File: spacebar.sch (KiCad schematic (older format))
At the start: 16 parts

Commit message: Flip some spacebars
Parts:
- K_SP1, K_SP3: footprint MX_Alps_Hybrid:MX-7U -> MX_Alps_Hybrid:MX-7U-ReversedStabilizers
- K_SP2: footprint MX_Alps_Hybrid:MX-6.25U -> MX_Alps_Hybrid:MX-6.25U-ReversedStabilizers
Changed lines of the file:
@@
 F 0 "K_SP2" H 5150 1450 60  0000 C CNN
 F 1 "MX-6.25U" H 5150 1375 20  0000 C CNN
-F 2 "MX_Alps_Hybrid:MX-6.25U" H 5125 1300 60  0001 C CNN
+F 2 "MX_Alps_Hybrid:MX-6.25U-ReversedStabilizers" H 5125 1300 60  0001 C CNN
 F 3 "" H 5125 1300 60  0001 C CNN
 	1    5150 1325
@@
 F 0 "K_SP1" H 5125 5650 60  0000 C CNN
 F 1 "MX-7U" H 5125 5575 20  0000 C CNN
-F 2 "MX_Alps_Hybrid:MX-7U" H 5100 5500 60  0001 C CNN
+F 2 "MX_Alps_Hybrid:MX-7U-ReversedStabilizers" H 5100 5500 60  0001 C CNN
 F 3 "" H 5100 5500 60  0001 C CNN
 	1    5125 5525
@@
 F 0 "K_SP3" H 5125 6175 60  0000 C CNN
 F 1 "MX-7U" H 5125 6100 20  0000 C CNN
-F 2 "MX_Alps_Hybrid:MX-7U" H 5100 6025 60  0001 C CNN
+F 2 "MX_Alps_Hybrid:MX-7U-ReversedStabilizers" H 5100 6025 60  0001 C CNN
 F 3 "" H 5100 6025 60  0001 C CNN
 	1    5125 6050

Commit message: Add dummy 6U hole schematic
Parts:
- added K_SP3_ExtraStabs: MX-6U-STABS, symbol MX-ISO
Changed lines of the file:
@@
 	5375 6525 4875 6525
 Connection ~ 4925 6450
+$Comp
+L MX-ISO K_SP3_ExtraStabs
+U 1 1 598719D6
+P 5100 7100
+F 0 "K_SP3_ExtraStabs" H 5100 7225 60  0000 C CNN
+F 1 "MX-6U-STABS" H 5100 7150 20  0000 C CNN
+F 2 "" H 5075 7075 60  0001 C CNN
+F 3 "" H 5075 7075 60  0001 C CNN
+	1    5100 7100
+	1    0    0    -1
+$EndComp
 $EndSCHEMATC

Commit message: Stack bottom row, move HHKB layout out of the way temporarily
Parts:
- removed K_SP3_ExtraStabs: MX-6U-STABS, symbol MX-ISO
- added K_SP3_Extra1: MX-6U, MX_Alps_Hybrid:MX-6U-7UOverlay, symbol MX-6U
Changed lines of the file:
@@
 Connection ~ 4925 6450
 $Comp
-L MX-ISO K_SP3_ExtraStabs
-U 1 1 598719D6
-P 5100 7100
-F 0 "K_SP3_ExtraStabs" H 5100 7225 60  0000 C CNN
-F 1 "MX-6U-STABS" H 5100 7150 20  0000 C CNN
-F 2 "" H 5075 7075 60  0001 C CNN
-F 3 "" H 5075 7075 60  0001 C CNN
-	1    5100 7100
+L MX-6U K_SP3_Extra1
+U 1 1 5987A302
+P 6725 3400
+F 0 "K_SP3_Extra1" H 6725 3525 60  0000 C CNN
+F 1 "MX-6U" H 6725 3450 20  0000 C CNN
+F 2 "MX_Alps_Hybrid:MX-6U-7UOverlay" H 6700 3375 60  0001 C CNN
+F 3 "" H 6700 3375 60  0001 C CNN
+	1    6725 3400
 	1    0    0    -1
 $EndComp

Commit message: Fix 2.25 and 2.75U flipped stabilizer holes
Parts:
- K_SP11, K_SP5, K_SP8: footprint MX_Alps_Hybrid:MX-2.75U -> MX_Alps_Hybrid:MX-2.75U-ReversedStabilizer
- K_SP6, K_SP7: footprint MX_Alps_Hybrid:MX-2.25U -> MX_Alps_Hybrid:MX-2.25U-ReversedStabilizer
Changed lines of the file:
@@
 F 0 "K_SP5" H 4700 1975 60  0000 C CNN
 F 1 "MX-2.75U" H 4700 1900 20  0000 C CNN
-F 2 "MX_Alps_Hybrid:MX-2.75U" H 4675 1825 60  0001 C CNN
+F 2 "MX_Alps_Hybrid:MX-2.75U-ReversedStabilizer" H 4675 1825 60  0001 C CNN
 F 3 "" H 4675 1825 60  0001 C CNN
 	1    4700 1850
@@
 F 0 "K_SP7" H 5600 1975 60  0000 C CNN
 F 1 "MX-2.25U" H 5600 1900 20  0000 C CNN
-F 2 "MX_Alps_Hybrid:MX-2.25U" H 5575 1825 60  0001 C CNN
+F 2 "MX_Alps_Hybrid:MX-2.25U-ReversedStabilizer" H 5575 1825 60  0001 C CNN
 F 3 "" H 5575 1825 60  0001 C CNN
 	1    5600 1850
@@
 F 0 "K_SP6" H 4700 2500 60  0000 C CNN
 F 1 "MX-2.25U" H 4700 2425 20  0000 C CNN
-F 2 "MX_Alps_Hybrid:MX-2.25U" H 4675 2350 60  0001 C CNN
+F 2 "MX_Alps_Hybrid:MX-2.25U-ReversedStabilizer" H 4675 2350 60  0001 C CNN
 F 3 "" H 4675 2350 60  0001 C CNN
 	1    4700 2375
@@
 F 0 "K_SP8" H 5600 2500 60  0000 C CNN
 F 1 "MX-2.75U" H 5600 2425 20  0000 C CNN
-F 2 "MX_Alps_Hybrid:MX-2.75U" H 5575 2350 60  0001 C CNN
+F 2 "MX_Alps_Hybrid:MX-2.75U-ReversedStabilizer" H 5575 2350 60  0001 C CNN
 F 3 "" H 5575 2350 60  0001 C CNN
 	1    5600 2375
@@
 F 0 "K_SP11" H 4700 3550 60  0000 C CNN
 F 1 "MX-2.75U" H 4700 3475 20  0000 C CNN
-F 2 "MX_Alps_Hybrid:MX-2.75U" H 4675 3400 60  0001 C CNN
+F 2 "MX_Alps_Hybrid:MX-2.75U-ReversedStabilizer" H 4675 3400 60  0001 C CNN
 F 3 "" H 4675 3400 60  0001 C CNN
 	1    4700 3425

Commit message: Get rid of LM5 and SP1 for 6.5U bottom row
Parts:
- removed K_SP1: MX-7U, MX_Alps_Hybrid:MX-7U-ReversedStabilizers, symbol MX-7U
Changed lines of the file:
@@
-$EndComp
-$Comp
-L MX-7U K_SP1
-U 1 1 594AF20B
-P 5125 5525
-F 0 "K_SP1" H 5125 5650 60  0000 C CNN
-F 1 "MX-7U" H 5125 5575 20  0000 C CNN
-F 2 "MX_Alps_Hybrid:MX-7U-ReversedStabilizers" H 5100 5500 60  0001 C CNN
-F 3 "" H 5100 5500 60  0001 C CNN
-	1    5125 5525
-	1    0    0    -1
 $EndComp
 $Comp

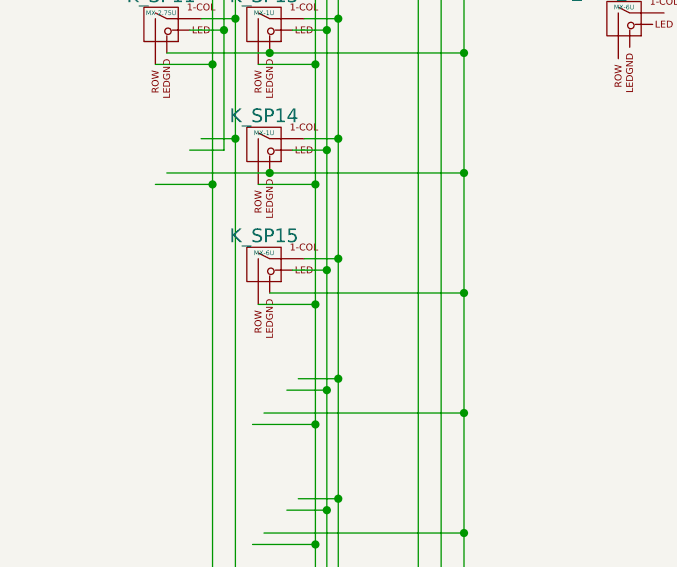
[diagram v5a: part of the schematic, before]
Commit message: Remove true HHKB row (LM8/9, SP15, RM15/16)
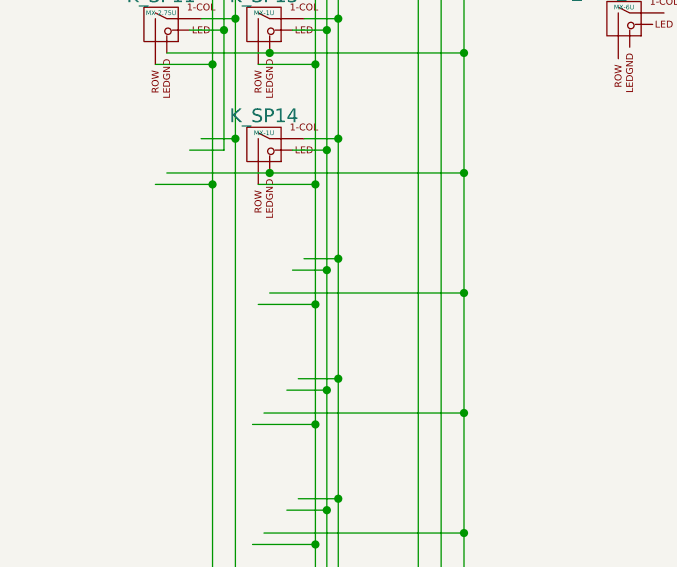
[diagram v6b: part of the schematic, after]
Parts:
- removed K_SP15: MX-6U, MX_Alps_Hybrid:MX-6U, symbol MX-6U
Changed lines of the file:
@@
-$EndComp
-$Comp
-L MX-6U K_SP15
-U 1 1 594AEB53
-P 5150 4475
-F 0 "K_SP15" H 5150 4600 60  0000 C CNN
-F 1 "MX-6U" H 5150 4525 20  0000 C CNN
-F 2 "MX_Alps_Hybrid:MX-6U" H 5125 4450 60  0001 C CNN
-F 3 "" H 5125 4450 60  0001 C CNN
-	1    5150 4475
-	1    0    0    -1
 $EndComp
 $Comp

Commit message: Remove SP14, clean up PCB
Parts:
- removed K_SP14: MX-1U, MX_Alps_Hybrid:MX-1U, symbol MX-1U
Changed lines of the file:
@@
-$EndComp
-$Comp
-L MX-2.75U K_SP5
-U 1 1 594AD90C
-P 4700 1850
-F 0 "K_SP5" H 4700 1975 60  0000 C CNN
-F 1 "MX-2.75U" H 4700 1900 20  0000 C CNN
-F 2 "MX_Alps_Hybrid:MX-2.75U-ReversedStabilizer" H 4675 1825 60  0001 C CNN
-F 3 "" H 4675 1825 60  0001 C CNN
-	1    4700 1850
-	1    0    0    -1
 $EndComp
 $Comp
@@
 F 3 "" H 5125 3400 60  0001 C CNN
 	1    5150 3425
-	1    0    0    -1
-$EndComp
-$Comp
-L MX-1U K_SP14
-U 1 1 594AE7A9
-P 5150 3950
-F 0 "K_SP14" H 5150 4075 60  0000 C CNN
-F 1 "MX-1U" H 5150 4000 20  0000 C CNN
-F 2 "MX_Alps_Hybrid:MX-1U" H 5125 3925 60  0001 C CNN
-F 3 "" H 5125 3925 60  0001 C CNN
-	1    5150 3950
 	1    0    0    -1
 $EndComp
@@
 	1    0    0    -1
 $EndComp
+$Comp
+L MX-2.75U K_SP5
+U 1 1 594AD90C
+P 4700 1850
+F 0 "K_SP5" H 4700 1975 60  0000 C CNN
+F 1 "MX-2.75U" H 4700 1900 20  0000 C CNN
+F 2 "MX_Alps_Hybrid:MX-2.75U-ReversedStabilizer" H 4675 1825 60  0001 C CNN
+F 3 "" H 4675 1825 60  0001 C CNN
+	1    4700 1850
+	1    0    0    -1
+$EndComp

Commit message: Add 7U Split Spacebar
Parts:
- added K_SP14: MX-2U, MX_Alps_Hybrid:MX-2U-ReversedStabilizers, symbol MX-2U
- added K_SP15: MX-2.25U, MX_Alps_Hybrid:MX-2.25U-ReversedStabilizer, symbol MX-2.25U
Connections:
- wire segments 76 -> 79
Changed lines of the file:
@@
 	5725 1875 5875 1875
 Wire Wire Line
-	5875 1125 5875 2400
+	5875 1125 5875 2925
 Wire Wire Line
 	5875 2400 5725 2400
@@
 	1    0    0    -1
 $EndComp
+$Comp
+L MX-2U K_SP14
+U 1 1 598952D9
+P 5150 2900
+F 0 "K_SP14" H 5150 3025 60  0000 C CNN
+F 1 "MX-2U" H 5150 2950 20  0000 C CNN
+F 2 "MX_Alps_Hybrid:MX-2U-ReversedStabilizers" H 5125 2875 60  0001 C CNN
+F 3 "" H 5125 2875 60  0001 C CNN
+	1    5150 2900
+	1    0    0    -1
+$EndComp
+$Comp
+L MX-2.25U K_SP15
+U 1 1 598954D5
+P 5600 2900
+F 0 "K_SP15" H 5600 3025 60  0000 C CNN
+F 1 "MX-2.25U" H 5600 2950 20  0000 C CNN
+F 2 "MX_Alps_Hybrid:MX-2.25U-ReversedStabilizer" H 5575 2875 60  0001 C CNN
+F 3 "" H 5575 2875 60  0001 C CNN
+	1    5600 2900
+	1    0    0    -1
+$EndComp
+Connection ~ 5625 3025
+Wire Wire Line
+	5775 2875 5925 2875
+Connection ~ 5925 2875
+Wire Wire Line
+	5575 3075 5825 3075
+Connection ~ 5825 3075
+Wire Wire Line
+	5875 2925 5725 2925
+Connection ~ 5875 2400
 $EndSCHEMATC
